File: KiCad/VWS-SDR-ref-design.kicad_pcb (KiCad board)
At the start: 4 copper layers, 100 x 100 mm, 99 parts, among them J1 RF_IN, J10 IF breakout, J2 IQ_Out, J3 SI5351 board, J6 I2C breakout, J7 Power breakout, J8 GPIO Breakout, J9 GPIO Breakout, U1 GALI-S66, U2 74CBTLV3253DR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

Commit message: Layout complete
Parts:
- moved J6 30.7 mm to (118.4, 111.0)
- moved J1 0.26 mm to (73.7, 54.8)
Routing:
- net +5V: track 0.00 -> 234.2 mm, vias 0 -> 3
- net +3V3: track 0.00 -> 102.7 mm, vias 0 -> 2
- net /CLK0: track 0.00 -> 91.9 mm, vias 0 -> 2
- net /SCL: track 0.00 -> 90.2 mm
- net /CLK1: track 0.00 -> 88.5 mm, vias 0 -> 2
- net /SDA: track 0.00 -> 87.7 mm
- net /I_out: track 0.00 -> 57.7 mm
- net GND: track 0.00 -> 45.7 mm, vias 0 -> 555
- net Net-(U2-1B3): track 0.00 -> 38.8 mm, vias 0 -> 2
- net Net-(U2-1B2): track 0.00 -> 37.7 mm, vias 0 -> 2
- net Net-(R10-Pad2): track 0.00 -> 33.5 mm, vias 0 -> 2
- net Net-(U3A-+): track 0.00 -> 30.5 mm, vias 0 -> 2
- net /Q_out: track 0.00 -> 28.7 mm
- net Net-(U2-1B4): track 0.00 -> 27.8 mm, vias 0 -> 2
- net Net-(U2-1A): track 0.00 -> 26.1 mm
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- added copper zone on B.Cu, net GND
- added copper zone on F.Cu, net GND
- added copper zone on In1.Cu, net GND
- added copper zone on In2.Cu, net GND

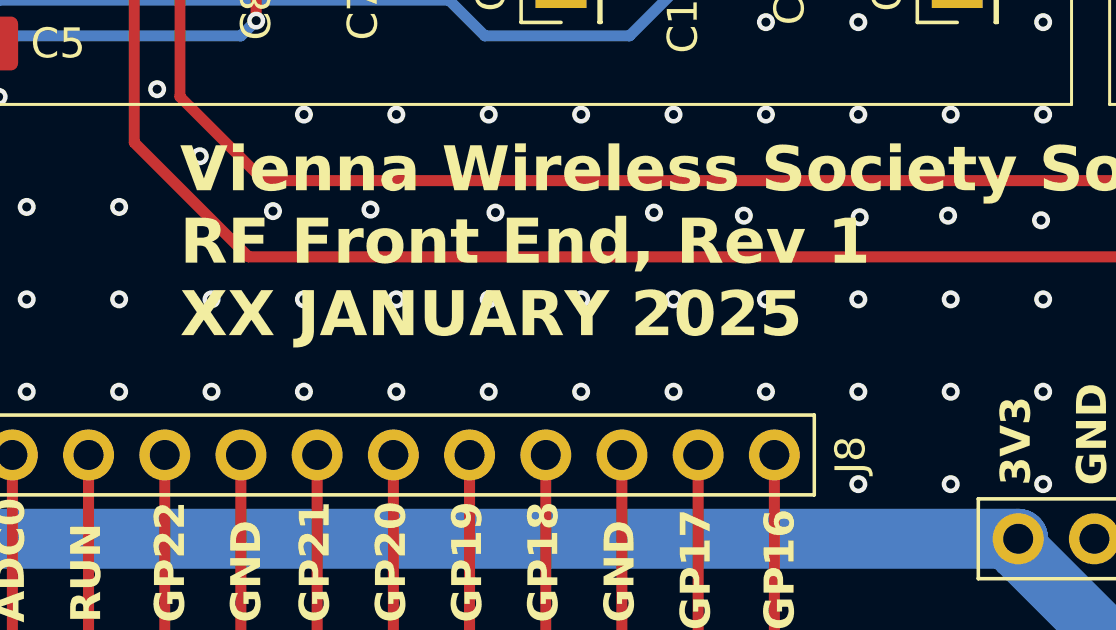
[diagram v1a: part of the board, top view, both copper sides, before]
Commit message: Added part selection
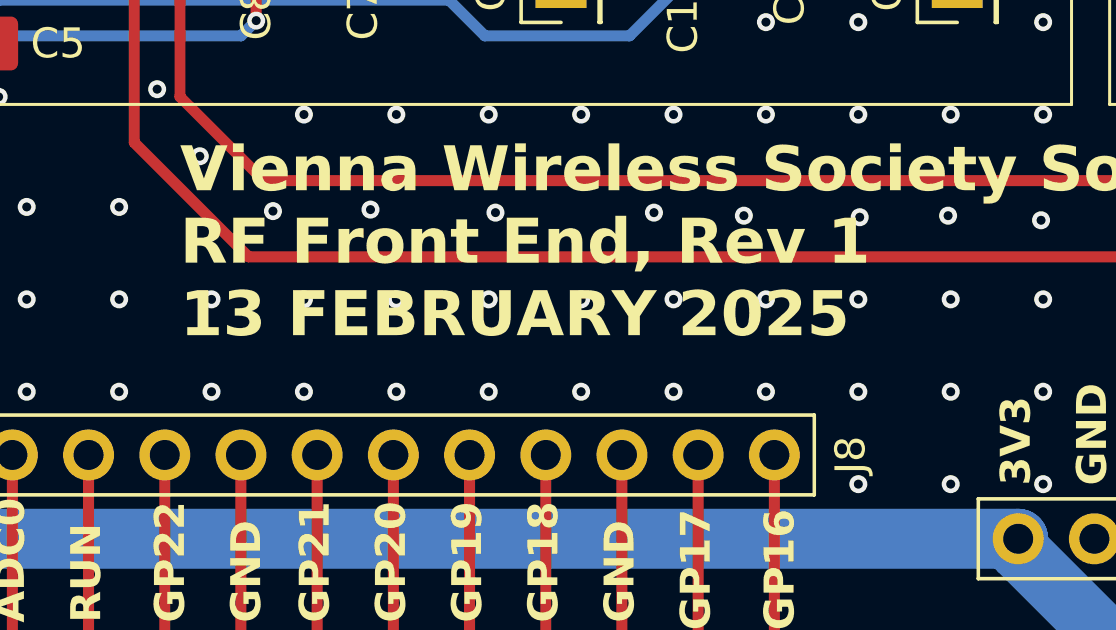
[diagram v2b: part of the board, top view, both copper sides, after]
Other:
- board text added: "Vienna Wireless Society Software Defined Receiver RF Front End, Rev 1 13 FEBRUARY 2025"
- board text removed: "Vienna Wireless Society Software Defined Receiver RF Front End, Rev 1 XX JANUARY 2025"
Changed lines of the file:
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@@
 		)
 	)
-	(gr_text "Vienna Wireless Society Software Defined Receiver\nRF Front End, Rev 1\nXX JANUARY 2025"
+	(gr_text "Vienna Wireless Society Software Defined Receiver\nRF Front End, Rev 1\n13 FEBRUARY 2025"
 		(at 82.804 104.394 0)
 		(layer "F.SilkS")

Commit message: Update for Rev 2 of the board
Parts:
- added D1: 5V LED, LED_SMD:LED_1206_3216Metric_Pad1.42x1.75mm_HandSolder, F.Cu at (53.3, 87.6)
- added D2: 3V3 LED, LED_SMD:LED_1206_3216Metric_Pad1.42x1.75mm_HandSolder, F.Cu at (77.5, 101.6)
- added D3: Indicator, LED_SMD:LED_1206_3216Metric_Pad1.42x1.75mm_HandSolder, F.Cu at (106.2, 104.4)
- added R26: 3k, Resistor_SMD:R_1206_3216Metric_Pad1.30x1.75mm_HandSolder, F.Cu at (53.3, 82.0)
- added R27: 1k5, Resistor_SMD:R_1206_3216Metric_Pad1.30x1.75mm_HandSolder, F.Cu at (80.5, 101.6)
- added R28: 1k5, Resistor_SMD:R_1206_3216Metric_Pad1.30x1.75mm_HandSolder, F.Cu at (112.0, 104.4)
- added TP19: TestPoint, Connector_PinHeader_2.54mm:PinHeader_1x01_P2.54mm_Vertical, F.Cu at (87.6, 94.5)
- added TP20: TestPoint, Connector_PinHeader_2.54mm:PinHeader_1x01_P2.54mm_Vertical, F.Cu at (101.9, 94.7)
- added a: LNA Bias, TestPoint:TestPoint_Pad_D1.5mm, F.Cu at (74.7, 72.6)
- added c: Mixer Enable, TestPoint:TestPoint_Pad_D1.5mm, F.Cu at (61.5, 79.8)
- added d: Mixer DC, TestPoint:TestPoint_Pad_D1.5mm, F.Cu at (61.5, 82.8)
- added e: Q offset, TestPoint:TestPoint_Pad_D1.5mm, F.Cu at (85.6, 71.6)
- added f: I offset, TestPoint:TestPoint_Pad_D1.5mm, F.Cu at (111.3, 71.6)
- added g: Amp DC, TestPoint:TestPoint_Pad_D1.5mm, F.Cu at (100.3, 62.0)
- added h: Filter DC, TestPoint:TestPoint_Pad_D1.5mm, F.Cu at (137.7, 81.5)
- J8: value GPIO Breakout -> GPIO Breakout1
- J9: value GPIO Breakout -> GPIO Breakout2
- renumbered TP1 to TP1/b
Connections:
- J10 pad 2: /I_out -> GND
- J10 pad 3: GND -> /I_out
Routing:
- net +5V: track 234.2 -> 243.2 mm
- net +3V3: track 102.7 -> 111.7 mm
- net Net-(C10-Pad1): track 6.04 -> 13.9 mm
- net Net-(C12-Pad2): track 6.00 -> 13.6 mm
- net GND: track 45.7 -> 53.2 mm, vias 555 -> 371
- net Net-(U3C-V+): track 19.8 -> 25.5 mm
- net /I_out: track 57.7 -> 62.7 mm
- net Net-(D3-A): track 9.15 -> 13.8 mm
- net Net-(U2-1~{OE}): track 11.4 -> 15.7 mm
- net Net-(C4-Pad1): track 9.01 -> 12.8 mm
- net Net-(U3A-+): track 30.5 -> 34.3 mm
- net Net-(U3B-+): track 26.1 -> 29.3 mm
- net Net-(D2-K): track 0.00 -> 3.07 mm
- net Net-(U4C-V+): track 7.23 -> 10.1 mm
- net Net-(D3-K): track 0.00 -> 2.80 mm
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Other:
- board text added: "I+"
- board text added: "IF Amplifier"
- board text added: "KM4UDX LED"
- board text added: "Lowpass Filter"
- board text added: "Q+"
- board text added: "Vienna Wireless Society Software Defined Receiver RF Front End, Rev 2, 1 MARCH 2025"
- board text removed: "Low pass filter"
- board text removed: "Vienna Wireless Society Software Defined Receiver RF Front End, Rev 1 13 FEBRUARY 2025"
